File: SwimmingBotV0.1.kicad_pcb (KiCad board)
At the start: 2 copper layers, 70 x 51 mm, 137 parts, among them P10 ANT, P11 DEBUG, P2 ANALOG, P3 CHRG, P4 BATT, P5 DEBUG_JUMPER, P6 FIN1, P7 FIN2, P8 MOT1, P9 MOT2, Q1 Q_NMOS_DGS, Q10 PMV45EN2, Q11 PMV45EN2, Q12 PMV45EN2, Q13 PMV45EN2, Q14 PMV45EN2, Q15 PMV45EN2, Q2 Q_PMOS_DGS, Q3 Q_NMOS_DGS, Q4 PMV45EN2, Q5 PMV45EN2, Q6 PMV45EN2, Q7 PMV45EN2, Q8 PMV45EN2, Q9 PMV45EN2, U1 LT3470A, U10 TPS6216X, U2 MCP73834, U3 A4960, U4 A4960, U5 HUM-900-PRO, U6 MPU-9250, U8 MAX6034_25, U9 STM32F446-144, X1 CRYSTAL_SMD, Y1 Crystal

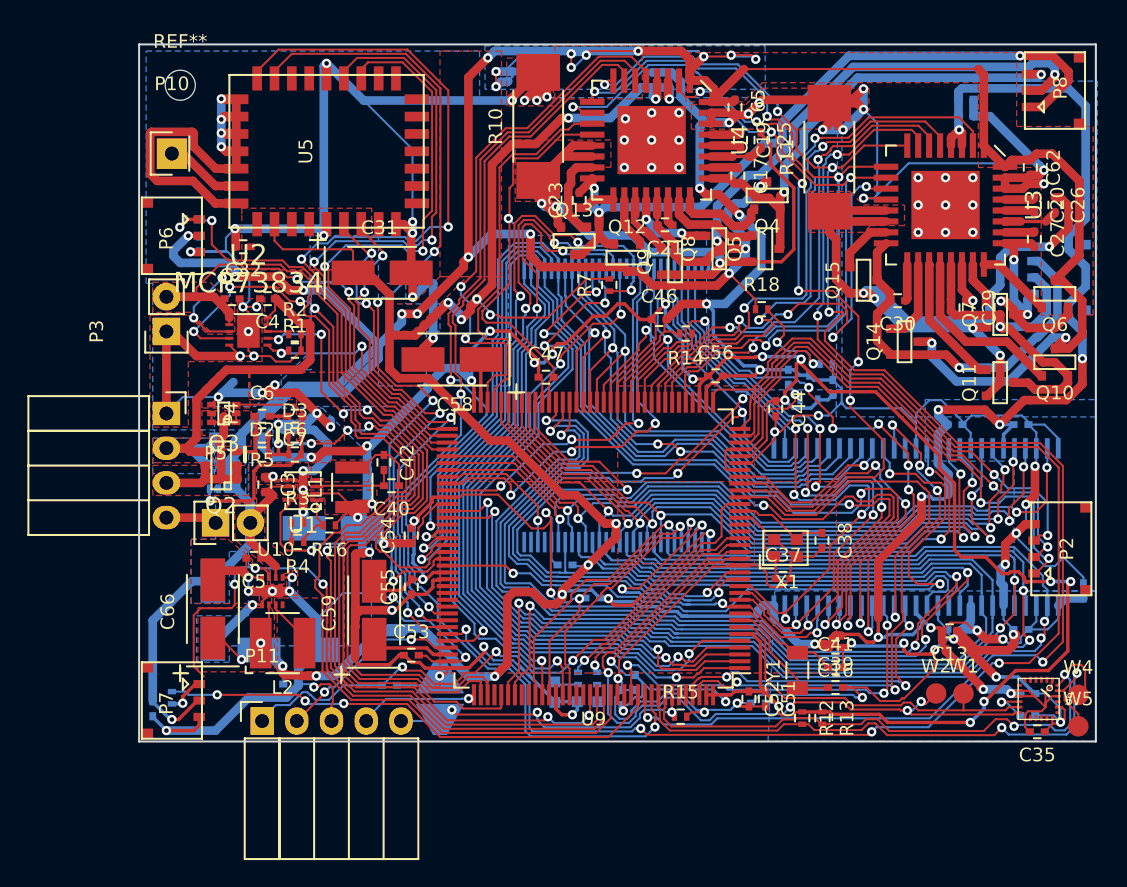
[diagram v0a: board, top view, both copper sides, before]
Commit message: silkscreen and mask layers fixed, working on paste
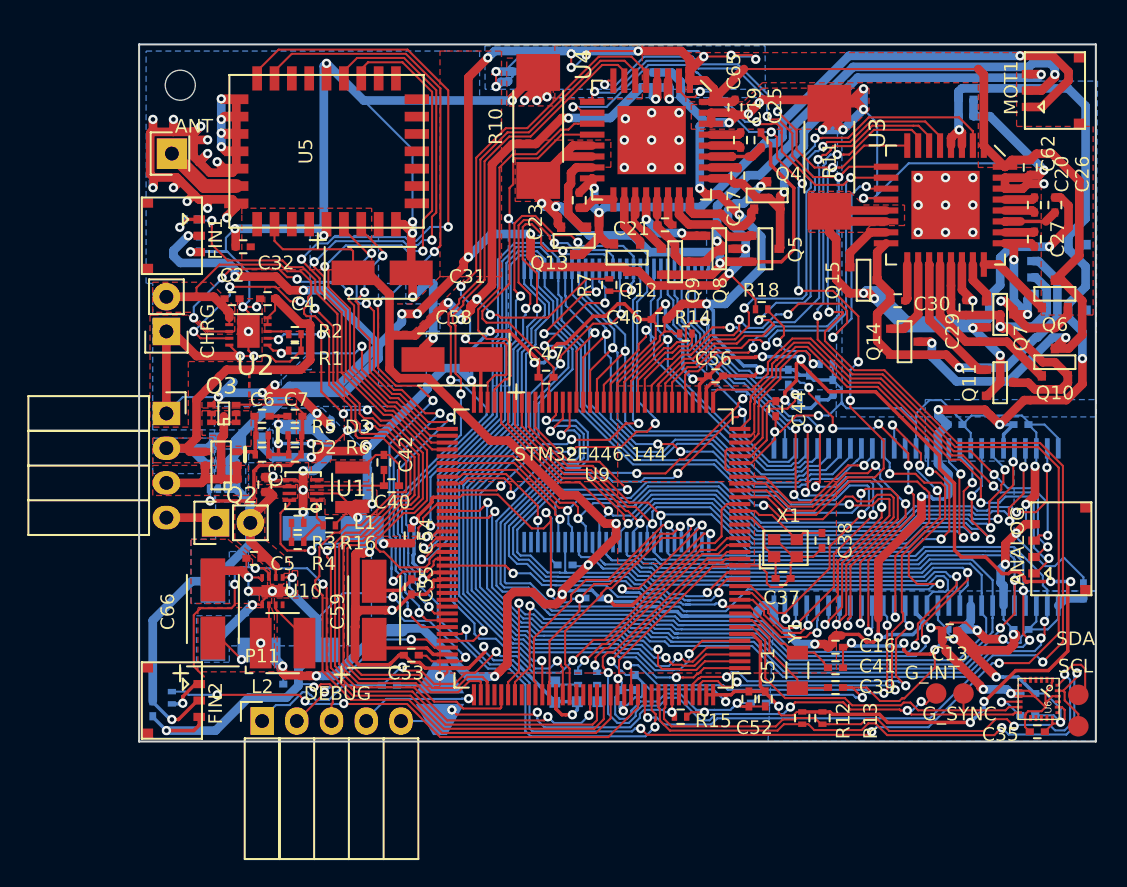
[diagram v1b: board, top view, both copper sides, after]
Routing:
- net GND: track 630.1 -> 642.9 mm, vias 79 -> 90
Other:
- rule pad_to_mask_clearance: 0.2 -> 0.0508
